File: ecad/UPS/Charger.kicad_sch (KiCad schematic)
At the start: 0 parts

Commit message: Misc repo cleanup
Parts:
- added C1, C13, C14, C15, C16, C17, C2, C3, C4: C, symbol Device:C
- added L1: L, symbol Device:L
- added Q1, Q2, Q3, Q4: NMOS, symbol Simulation_SPICE:NMOS
- added R1, R10, R11, R2, R3, R4, R5, R9: R, symbol Device:R
- added U1: BQ25731RSNR, RSN0032B-IPC_A, symbol UPS:BQ25731RSNR
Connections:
- new net: C14.1, C15.2, R10.1, U1.3 (ACP)
- new net: C13.1, C14.2, R9.1, U1.2 (ACN)
- new net: C16.2, L1.1, Q1.3 (S), Q2.1 (D)
- new net: R2.1, U1.10 (PSYS)
- new net: C1.1, U1.9 (IBAT)
- new net: Q1.1 (D), R11.1, R9.2
- new net: Q1.2 (G), U1.31 (HIDRV1)
- new net: Q4.1 (D), U1.22 (VSYS)
- new net: Q4.2 (G), U1.24 (HIDRV2)
- new net: C17.2, L1.2, Q3.1 (D), Q4.3 (S), U1.23 (SW2)
- new net: Q3.2 (G), U1.26 (LODRV2)
- new net: C2.1, R1.1, U1.8 (IADPT)
- new net: Q2.2 (G), U1.29 (LODRV1)
- new net BTST1: C16.1, U1.30 (BTST1)
- new net BTST2: C17.1, U1.25 (BTST2)
- new net GND: C1.2, C13.2, C15.1, C2.2, C3.2, C4.2, Q2.3 (S), Q3.3 (S), R1.2, R2.2, R3.2, U1.5 (OTG_VAP)
- new net ILIM_HIZ: R3.1, R4.2, U1.6 (ILIM_HIZ)
- new net PGND: U1.27 (PGND)
- new net REGN: C3.1, R5.1, U1.28 (REGN)
- new net VBUS_IN: R10.2, R11.2, U1.1 (VBUS)
- new net VDDA: C4.1, R4.1, R5.2, U1.7 (VDDA)
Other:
- company: (none) -> MTU Open Source Hardware Enterprise
- title: (none) -> Battery Management

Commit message: Update Symbols and Assign Footprints
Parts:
- U1: footprint RSN0032B-IPC_A -> UPS:RSN0032B-IPC_A
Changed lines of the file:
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@@
 			)
 		)
-		(property "Footprint" "RSN0032B-IPC_A"
+		(property "Footprint" "UPS:RSN0032B-IPC_A"
 			(at 115.57 43.18 0)
 			(effects

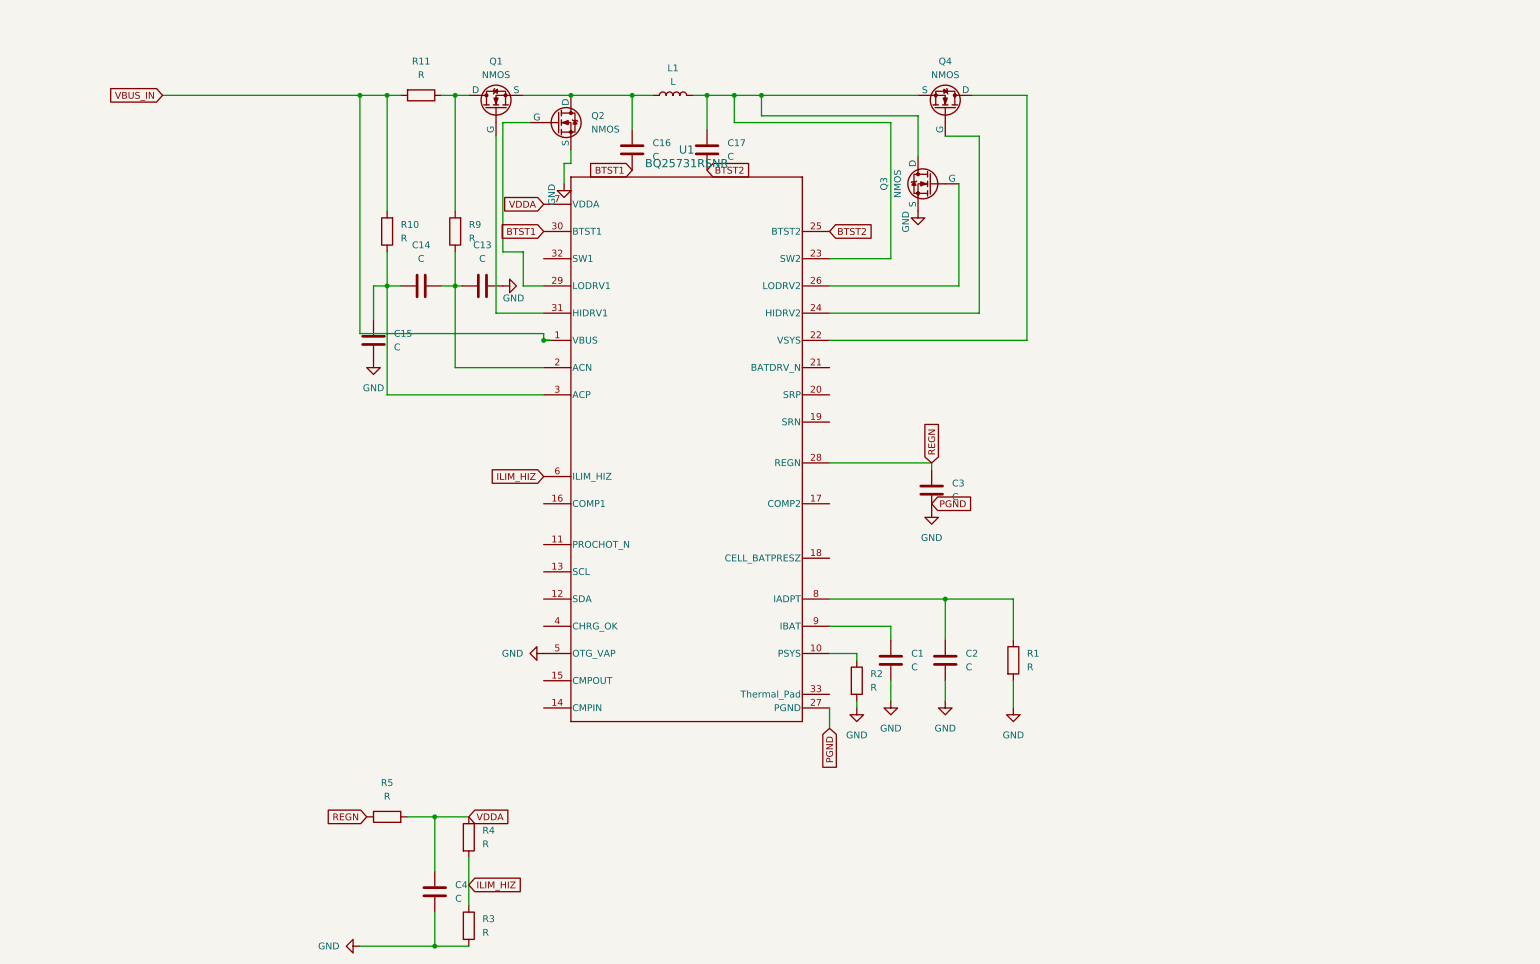
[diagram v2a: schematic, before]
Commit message: mcJohn
STM32L152RCT6 schematic and CubeIDE project
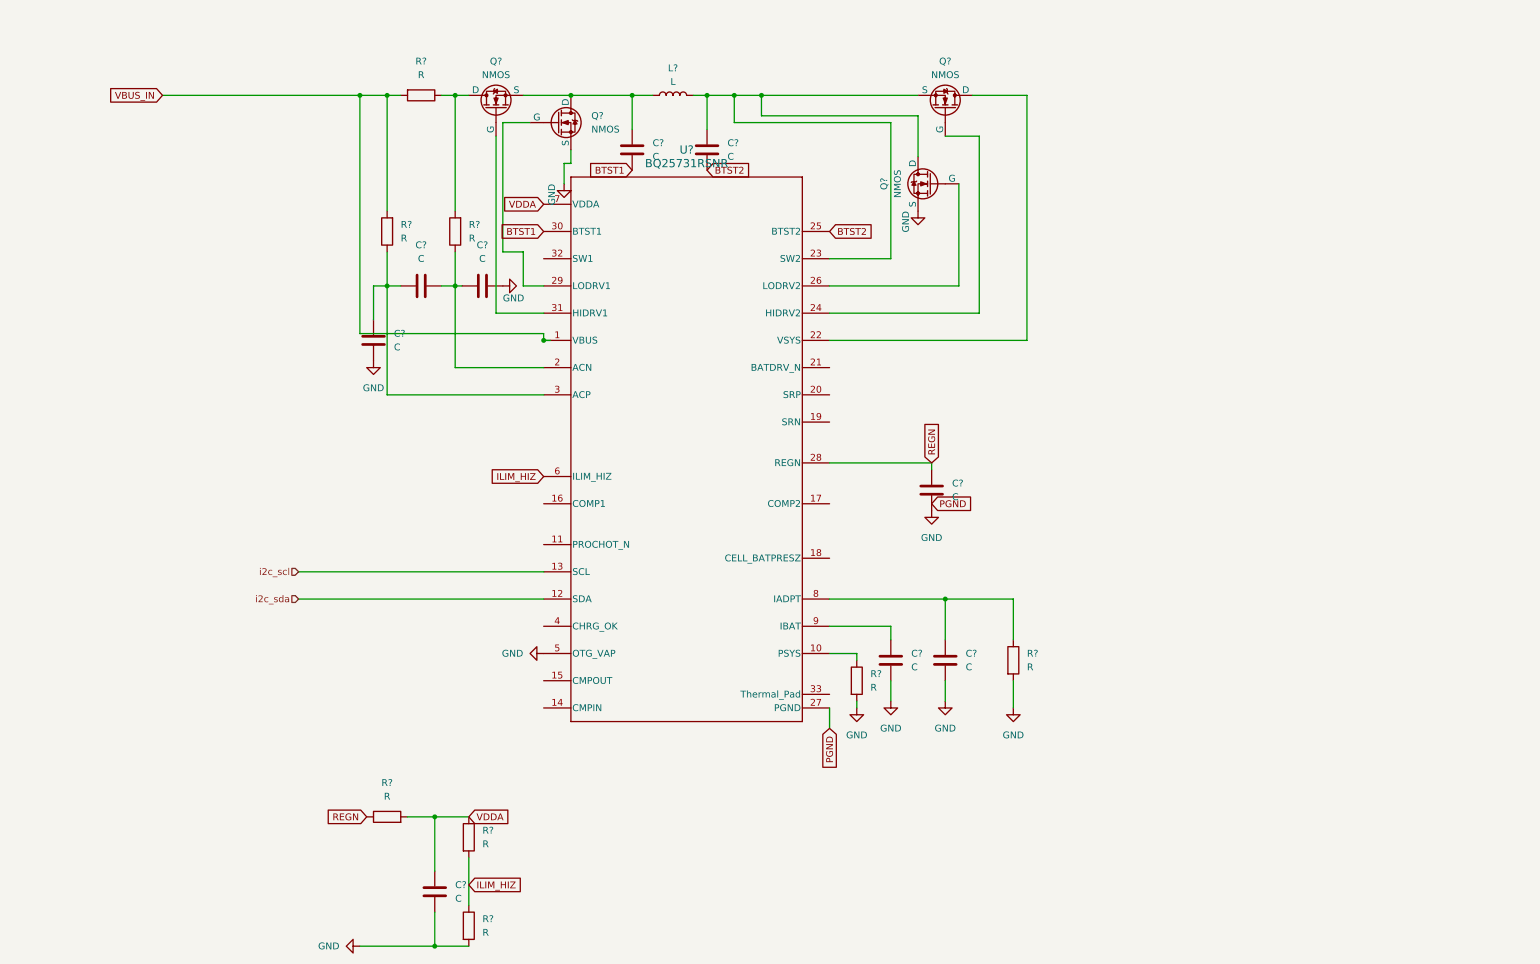
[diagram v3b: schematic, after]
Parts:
- renumbered C14 to C?, C4 to C?, C16 to C?, C1 to C?, C15 to C?, C13 to C?, C2 to C?, C17 to C?, C3 to C?, L1 to L?, Q1 to Q?, Q4 to Q?, Q3 to Q?, Q2 to Q?, R5 to R?, R2 to R?, R11 to R?, R3 to R?, R9 to R?, R10 to R?, R4 to R?, R1 to R?, U1 to U?
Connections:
- net i2c_sda: now reaches U?.12 (SDA)
- net i2c_scl: now reaches U?.13 (SCL)

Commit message: Cleanup
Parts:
- gave numbers to parts that had none: 23
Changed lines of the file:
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@@
 		(dnp no)
 		(fields_autoplaced yes)
-		(property "Reference" "C?"
+		(property "Reference" "C14"
 			(at 92.71 50.8 90)
 			(effects
@@
 		(dnp no)
 		(fields_autoplaced yes)
-		(property "Reference" "C?"
+		(property "Reference" "C4"
 			(at 99.06 170.1799 0)
 			(effects
@@
 		(dnp no)
 		(fields_autoplaced yes)
-		(property "Reference" "R?"
+		(property "Reference" "R5"
 			(at 86.36 151.13 90)
 			(effects
@@
 		(dnp no)
 		(fields_autoplaced yes)
-		(property "Reference" "C?"
+		(property "Reference" "C16"
 			(at 135.89 31.7499 0)
 			(effects
@@
 		(dnp no)
 		(fields_autoplaced yes)
-		(property "Reference" "R?"
+		(property "Reference" "R2"
 			(at 176.53 130.8099 0)
 			(effects
@@
 		(dnp no)
 		(fields_autoplaced yes)
-		(property "Reference" "C?"
+		(property "Reference" "C1"
 			(at 184.15 126.9999 0)
 			(effects
@@
 		(on_board yes)
 		(dnp no)
-		(property "Reference" "#PWR?"
+		(property "Reference" "#PWR017"
 			(at 185.42 50.8 0)
 			(effects
@@
 		(on_board yes)
 		(dnp no)
-		(property "Reference" "#PWR?"
+		(property "Reference" "#PWR015"
 			(at 114.3 58.42 0)
 			(effects
@@
 		(dnp no)
 		(fields_autoplaced yes)
-		(property "Reference" "#PWR?"
+		(property "Reference" "#PWR02"
 			(at 190.5 142.24 0)
 			(effects
@@
 		(dnp no)
 		(fields_autoplaced yes)
-		(property "Reference" "Q?"
+		(property "Reference" "Q1"
 			(at 106.68 16.51 90)
 			(effects
@@
 		(dnp no)
 		(fields_autoplaced yes)
-		(property "Reference" "#PWR?"
+		(property "Reference" "#PWR07"
 			(at 109.22 127 0)
 			(effects
@@
 		(on_board yes)
 		(dnp no)
-		(property "Reference" "Q?"
+		(property "Reference" "Q4"
 			(at 190.5 16.51 90)
 			(effects
@@
 		(dnp no)
 		(fields_autoplaced yes)
-		(property "Reference" "#PWR?"
+		(property "Reference" "#PWR05"
 			(at 187.96 106.68 0)
 			(effects
@@
 		(dnp no)
 		(fields_autoplaced yes)
-		(property "Reference" "R?"
+		(property "Reference" "R11"
 			(at 92.71 16.51 90)
 			(effects
@@
 		(dnp no)
 		(fields_autoplaced yes)
-		(property "Reference" "#PWR?"
+		(property "Reference" "#PWR014"
 			(at 83.82 78.74 0)
 			(effects
@@
 		(dnp no)
 		(fields_autoplaced yes)
-		(property "Reference" "#PWR?"
+		(property "Reference" "#PWR01"
 			(at 180.34 142.24 0)
 			(effects
@@
 		(dnp no)
 		(fields_autoplaced yes)
-		(property "Reference" "C?"
+		(property "Reference" "C15"
 			(at 87.63 67.3099 0)
 			(effects
@@
 		(dnp no)
 		(fields_autoplaced yes)
-		(property "Reference" "#PWR?"
+		(property "Reference" "#PWR04"
 			(at 173.99 143.51 0)
 			(effects
@@
 		(dnp no)
 		(fields_autoplaced yes)
-		(property "Reference" "R?"
+		(property "Reference" "R3"
 			(at 104.14 176.5299 0)
 			(effects
@@
 		(dnp no)
 		(fields_autoplaced yes)
-		(property "Reference" "#PWR?"
+		(property "Reference" "#PWR06"
 			(at 74.93 181.61 0)
 			(effects
@@
 		(dnp no)
 		(fields_autoplaced yes)
-		(property "Reference" "R?"
+		(property "Reference" "R9"
 			(at 101.6 46.9899 0)
 			(effects
@@
 		(dnp no)
 		(fields_autoplaced yes)
-		(property "Reference" "#PWR?"
+		(property "Reference" "#PWR03"
 			(at 203.2 143.51 0)
 			(effects
@@
 		(dnp no)
 		(fields_autoplaced yes)
-		(property "Reference" "L?"
+		(property "Reference" "L1"
 			(at 139.7 17.78 90)
 			(effects
@@
 		(dnp no)
 		(fields_autoplaced yes)
-		(property "Reference" "R?"
+		(property "Reference" "R10"
 			(at 88.9 46.9899 0)
 			(effects
@@
 		(dnp no)
 		(fields_autoplaced yes)
-		(property "Reference" "R?"
+		(property "Reference" "R4"
 			(at 104.14 160.0199 0)
 			(effects
@@
 		(on_board yes)
 		(dnp no)
-		(property "Reference" "Q?"
+		(property "Reference" "Q3"
 			(at 179.07 39.37 90)
 			(effects
@@
 		(dnp no)
 		(fields_autoplaced yes)
-		(property "Reference" "C?"
+		(property "Reference" "C13"
 			(at 104.14 50.8 90)
 			(effects
@@
 		(on_board yes)
 		(dnp no)
-		(property "Reference" "#PWR?"
+		(property "Reference" "#PWR016"
 			(at 119.38 45.72 0)
 			(effects
@@
 		(dnp no)
 		(fields_autoplaced yes)
-		(property "Reference" "C?"
+		(property "Reference" "C2"
 			(at 194.31 126.9999 0)
 			(effects
@@
 		(dnp no)
 		(fields_autoplaced yes)
-		(property "Reference" "C?"
+		(property "Reference" "C17"
 			(at 149.86 31.7499 0)
 			(effects
@@
 		(dnp no)
 		(fields_autoplaced yes)
-		(property "Reference" "R?"
+		(property "Reference" "R1"
 			(at 205.74 126.9999 0)
 			(effects
@@
 		(dnp no)
 		(fields_autoplaced yes)
-		(property "Reference" "Q?"
+		(property "Reference" "Q2"
 			(at 124.46 26.6699 0)
 			(effects
@@
 		(dnp no)
 		(fields_autoplaced yes)
-		(property "Reference" "U?"
+		(property "Reference" "U1"
 			(at 142.24 33.02 0)
 			(effects
@@
 		(dnp no)
 		(fields_autoplaced yes)
-		(property "Reference" "C?"
+		(property "Reference" "C3"
 			(at 191.77 95.2499 0)
 			(effects
